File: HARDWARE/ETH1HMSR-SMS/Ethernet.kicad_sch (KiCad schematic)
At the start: 34 parts, among them J301 RJ45_Wuerth_7499010121A, U301 LAN8742A, Y301 NX5032GA-25

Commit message: SW and HW development
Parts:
- removed R302, R304, R305: 33, Resistor_SMD:R_0603_1608Metric_Pad0.98x0.95mm_HandSolder, symbol Device:R
- removed R303, R306, R307, R308, R309: 10k, Resistor_SMD:R_0603_1608Metric_Pad0.98x0.95mm_HandSolder, symbol Device:R
- removed R313, R314, R315, R316: 49R9, Resistor_SMD:R_0603_1608Metric_Pad0.98x0.95mm_HandSolder, symbol Device:R
- added RN301: EXB-V8V103JV, Resistor_SMD:R_Array_Concave_4x0603, symbol Device:R_Pack04
- added RN302: EXB-V8V330JV, Resistor_SMD:R_Array_Concave_4x0603, symbol Device:R_Pack04
- added RN303: EXB-38V510JV, Resistor_SMD:R_Array_Concave_4x0603, symbol Device:R_Pack04
- R301: value 33 -> 10k
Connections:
- net +3.3V: now also RN301.5 (R4.2), RN301.6 (R3.2), RN301.7 (R2.2), RN301.8 (R1.2)
- net ETH_RXN: now also RN303.4 (R4.1)
- net ETH_RXP: now also RN303.3 (R3.1)
- net ETH_TXN: now also RN303.2 (R2.1)
- net ETH_TXP: now also RN303.1 (R1.1)
- net GND: now also R301.1
- net MODE0: now also RN301.1 (R1.1), RN302.8 (R1.2); no longer R301.1
- net MODE1: now also RN301.2 (R2.1), RN302.7 (R2.2)
- net MODE2: now also RN301.3 (R3.1), RN302.6 (R3.2)
- net REFCLK0: now also RN301.4 (R4.1), RN302.5 (R4.2)
- net REF_CLK: now also RN302.4 (R4.1)
- net RMII_CRS_DV: now also RN302.3 (R3.1)
- net RMII_RXD0: now also RN302.1 (R1.1); no longer R301.2
- net RMII_RXD1: now also RN302.2 (R2.1)
- net VCCQ: now also RN303.5 (R4.2), RN303.6 (R3.2), RN303.7 (R2.2), RN303.8 (R1.2)
- net at U301.10 (RXER/PHYAD0): now also R301.2
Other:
- moved on the sheet: C301, C302, C303, C304, C305, C306, C307, C308, C309, C310, C311, C312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

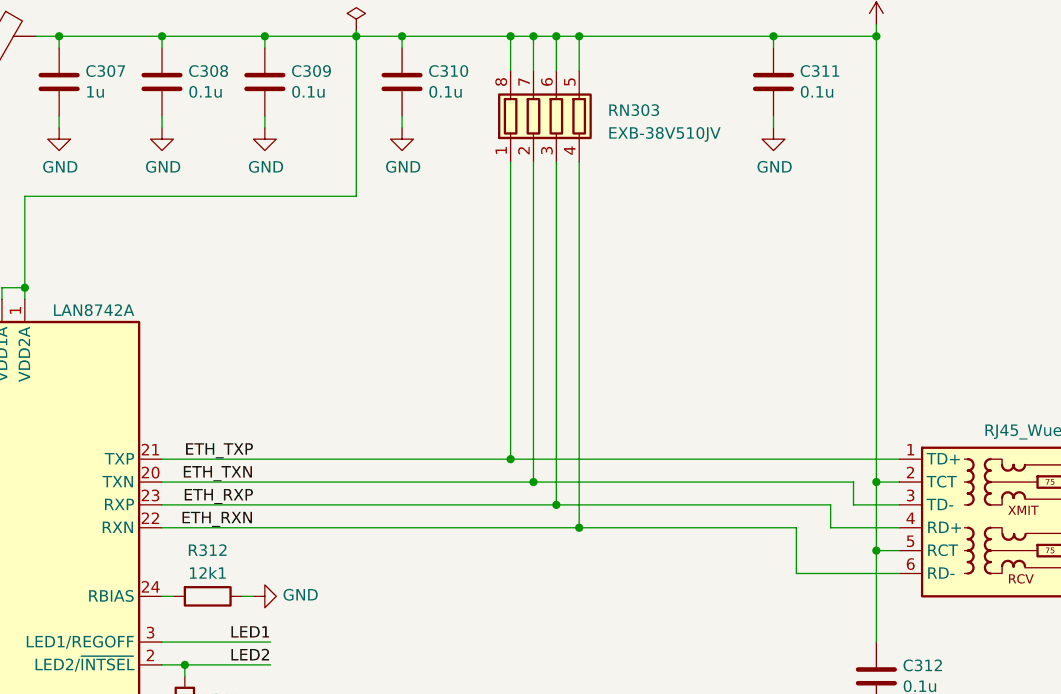
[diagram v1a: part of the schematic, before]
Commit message: Updated to Kicad 8
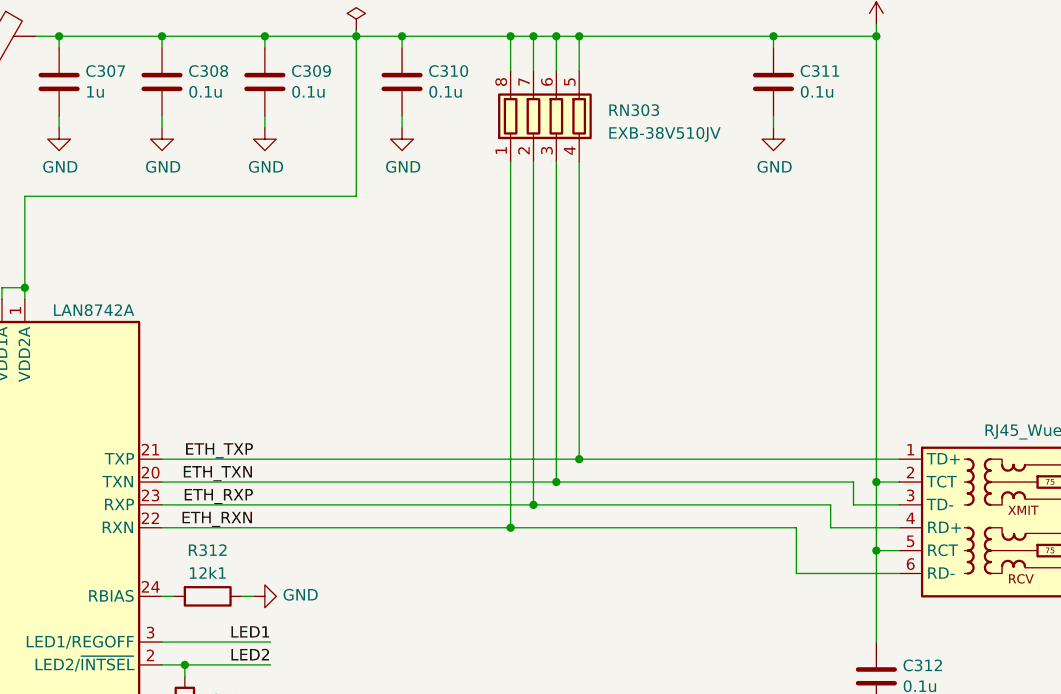
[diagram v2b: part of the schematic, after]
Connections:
- net ETH_RXN: now also RN303.1 (R1.1); no longer RN303.4 (R4.1)
- net ETH_RXP: now also RN303.2 (R2.1); no longer RN303.3 (R3.1)
- net ETH_TXN: now also RN303.3 (R3.1); no longer RN303.2 (R2.1)
- net ETH_TXP: now also RN303.4 (R4.1); no longer RN303.1 (R1.1)

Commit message: PCB design
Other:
- moved on the sheet: RN302
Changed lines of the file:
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@@
 	(wire
 		(pts
-			(xy 65.405 83.82) (xy 60.96 83.82)
+			(xy 67.31 83.82) (xy 60.96 83.82)
 		)
 		(stroke
@@
 	(wire
 		(pts
-			(xy 60.96 86.36) (xy 65.405 86.36)
+			(xy 60.96 86.36) (xy 67.31 86.36)
 		)
 		(stroke
@@
 	(wire
 		(pts
-			(xy 60.96 91.44) (xy 65.405 91.44)
+			(xy 60.96 91.44) (xy 67.31 91.44)
 		)
 		(stroke
@@
 	(wire
 		(pts
-			(xy 75.565 86.36) (xy 92.71 86.36)
+			(xy 77.47 86.36) (xy 92.71 86.36)
 		)
 		(stroke
@@
 	(wire
 		(pts
-			(xy 60.96 88.9) (xy 65.405 88.9)
+			(xy 60.96 88.9) (xy 67.31 88.9)
 		)
 		(stroke
@@
 	(wire
 		(pts
-			(xy 76.835 104.14) (xy 92.71 104.14)
+			(xy 78.74 104.14) (xy 92.71 104.14)
 		)
 		(stroke
@@
 	(wire
 		(pts
-			(xy 76.835 91.44) (xy 76.835 104.14)
+			(xy 78.74 91.44) (xy 78.74 104.14)
 		)
 		(stroke
@@
 	(wire
 		(pts
-			(xy 75.565 83.82) (xy 92.71 83.82)
+			(xy 77.47 83.82) (xy 92.71 83.82)
 		)
 		(stroke
@@
 	(wire
 		(pts
-			(xy 75.565 91.44) (xy 76.835 91.44)
+			(xy 77.47 91.44) (xy 78.74 91.44)
 		)
 		(stroke
@@
 	(wire
 		(pts
-			(xy 78.74 91.44) (xy 92.71 91.44)
+			(xy 80.01 91.44) (xy 92.71 91.44)
 		)
 		(stroke
@@
 	(wire
 		(pts
-			(xy 75.565 88.9) (xy 78.74 88.9)
+			(xy 77.47 88.9) (xy 80.01 88.9)
 		)
 		(stroke
@@
 	(wire
 		(pts
-			(xy 78.74 88.9) (xy 78.74 91.44)
+			(xy 80.01 88.9) (xy 80.01 91.44)
 		)
 		(stroke
@@
 	(symbol
 		(lib_id "Device:R_Pack04")
-		(at 70.485 88.9 270)
+		(at 72.39 88.9 270)
 		(unit 1)
 		(exclude_from_sim no)
@@
 		(dnp no)
 		(property "Reference" "RN302"
-			(at 64.135 82.55 90)
+			(at 64.516 82.55 90)
 			(effects
 				(font
@@
 		)
 		(property "Value" "EXB-V8V330JV"
-			(at 68.58 94.615 90)
+			(at 70.485 94.615 90)
 			(effects
 				(font
@@
 		)
 		(property "Footprint" "Resistor_SMD:R_Array_Concave_4x0603"
-			(at 70.485 95.885 90)
+			(at 72.39 95.885 90)
 			(effects
 				(font
@@
 		)
 		(property "Datasheet" "~"
-			(at 70.485 88.9 0)
+			(at 72.39 88.9 0)
 			(effects
 				(font
@@
 		)
 		(property "Description" ""
-			(at 70.485 88.9 0)
-			(effects
-				(font
+			(at 72.39 88.9 0)
+			(effects
+				(font

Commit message: Development
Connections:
- net LED1: now also J301.9; no longer J301.10
- net LED2: now also J301.11; no longer J301.12
- net at R317.1: now also J301.12; no longer J301.11
- net at R318.1: now also J301.10; no longer J301.9
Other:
- moved on the sheet: C301, C311, C312, J301, R301, R310, R317, R318, RN301, RN303

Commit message: PCB
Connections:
- net LED1: now also J301.10; no longer J301.9
- net LED2: now also J301.12; no longer J301.11
- net at R317.1: now also J301.11; no longer J301.12
- net at R318.1: now also J301.9; no longer J301.10
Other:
- moved on the sheet: R317, R318
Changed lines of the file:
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@@
 	(wire
 		(pts
-			(xy 256.54 88.9) (xy 257.81 88.9)
+			(xy 256.54 91.44) (xy 257.81 91.44)
 		)
 		(stroke
@@
 	(wire
 		(pts
-			(xy 256.54 78.74) (xy 257.81 78.74)
+			(xy 256.54 81.28) (xy 257.81 81.28)
 		)
 		(stroke
@@
 	(wire
 		(pts
-			(xy 273.05 82.55) (xy 257.81 82.55)
+			(xy 267.97 74.93) (xy 257.81 74.93)
 		)
 		(stroke
@@
 	(wire
 		(pts
-			(xy 257.81 81.28) (xy 256.54 81.28)
-		)
-		(stroke
-			(width 0)
-			(type default)
-		)
-	)
-	(wire
-		(pts
-			(xy 257.81 82.55) (xy 257.81 81.28)
-		)
-		(stroke
-			(width 0)
-			(type default)
-		)
-	)
-	(wire
-		(pts
 			(xy 210.82 31.75) (xy 210.82 81.28)
 		)
@@
 	(wire
 		(pts
+			(xy 257.81 78.74) (xy 257.81 74.93)
+		)
+		(stroke
+			(width 0)
+			(type default)
+		)
+	)
+	(wire
+		(pts
 			(xy 130.81 33.02) (xy 130.81 31.75)
 		)
@@
 	(wire
 		(pts
+			(xy 256.54 78.74) (xy 257.81 78.74)
+		)
+		(stroke
+			(width 0)
+			(type default)
+		)
+	)
+	(wire
+		(pts
 			(xy 152.4 31.75) (xy 142.24 31.75)
 		)
@@
 	(wire
 		(pts
-			(xy 273.05 92.71) (xy 257.81 92.71)
+			(xy 267.97 85.09) (xy 257.81 85.09)
 		)
 		(stroke
@@
 	(wire
 		(pts
-			(xy 257.81 92.71) (xy 257.81 91.44)
+			(xy 80.01 91.44) (xy 92.71 91.44)
 		)
 		(stroke
@@
 	(wire
 		(pts
-			(xy 80.01 91.44) (xy 92.71 91.44)
+			(xy 115.57 49.53) (xy 152.4 49.53)
 		)
 		(stroke
@@
 	(wire
 		(pts
-			(xy 115.57 49.53) (xy 152.4 49.53)
+			(xy 201.93 86.36) (xy 201.93 91.44)
 		)
 		(stroke
@@
 	(wire
 		(pts
-			(xy 201.93 86.36) (xy 201.93 91.44)
+			(xy 170.18 31.75) (xy 170.18 35.56)
 		)
 		(stroke
@@
 	(wire
 		(pts
-			(xy 170.18 31.75) (xy 170.18 35.56)
+			(xy 248.92 96.52) (xy 248.92 97.79)
 		)
 		(stroke
@@
 	(wire
 		(pts
-			(xy 248.92 96.52) (xy 248.92 97.79)
+			(xy 257.81 85.09) (xy 257.81 88.9)
 		)
 		(stroke
@@
 	(wire
 		(pts
-			(xy 77.47 88.9) (xy 80.01 88.9)
+			(xy 256.54 88.9) (xy 257.81 88.9)
 		)
 		(stroke
@@
 	(wire
 		(pts
-			(xy 172.72 83.82) (xy 205.74 83.82)
+			(xy 77.47 88.9) (xy 80.01 88.9)
 		)
 		(stroke
@@
 	(wire
 		(pts
-			(xy 96.52 162.56) (xy 99.06 162.56)
+			(xy 172.72 83.82) (xy 205.74 83.82)
 		)
 		(stroke
@@
 	(wire
 		(pts
-			(xy 205.74 86.36) (xy 213.36 86.36)
+			(xy 96.52 162.56) (xy 99.06 162.56)
 		)
 		(stroke
@@
 	(wire
 		(pts
-			(xy 257.81 91.44) (xy 256.54 91.44)
+			(xy 205.74 86.36) (xy 213.36 86.36)
 		)
 		(stroke
@@
 	)
 	(label "LED1"
-		(at 273.05 92.71 180)
+		(at 267.97 85.09 180)
 		(fields_autoplaced yes)
 		(effects
@@
 	)
 	(label "LED2"
-		(at 273.05 82.55 180)
+		(at 267.97 74.93 180)
 		(fields_autoplaced yes)
 		(effects
@@
 	(symbol
 		(lib_id "Device:R")
-		(at 261.62 78.74 90)
+		(at 261.62 81.28 90)
 		(unit 1)
 		(exclude_from_sim no)
@@
 		(dnp no)
 		(property "Reference" "R317"
-			(at 261.62 74.295 90)
+			(at 261.62 76.835 90)
 			(effects
 				(font
@@
 		)
 		(property "Value" "560"
-			(at 261.62 76.2 90)
+			(at 261.62 78.74 90)
 			(effects
 				(font
@@
 		)
 		(property "Footprint" "Resistor_SMD:R_0603_1608Metric_Pad0.98x0.95mm_HandSolder"
-			(at 261.62 80.518 90)
+			(at 261.62 83.058 90)
 			(effects
 				(font
@@
 		)
 		(property "Datasheet" "~"
-			(at 261.62 78.74 0)
+			(at 261.62 81.28 0)
 			(effects
 				(font
@@
 		)
 		(property "Description" ""
-			(at 261.62 78.74 0)
+			(at 261.62 81.28 0)
 			(effects
 				(font
@@
 	(symbol
 		(lib_id "power:GND")
-		(at 265.43 88.9 90)
+		(at 265.43 91.44 90)
 		(unit 1)
 		(exclude_from_sim no)
@@
 		(fields_autoplaced yes)
 		(property "Reference" "#PWR0322"
-			(at 271.78 88.9 0)
+			(at 271.78 91.44 0)
 			(effects
 				(font
@@
 		)
 		(property "Value" "GND"
-			(at 269.24 88.9 90)
+			(at 269.24 91.44 90)
 			(effects
 				(font
@@
 		)
 		(property "Footprint" ""
-			(at 265.43 88.9 0)
+			(at 265.43 91.44 0)
 			(effects
 				(font
@@
 		)
 		(property "Datasheet" ""
-			(at 265.43 88.9 0)
+			(at 265.43 91.44 0)
 			(effects
 				(font
@@
 		)
 		(property "Description" "Power symbol creates a global label with name \"GND\" , ground"
-			(at 265.43 88.9 0)
+			(at 265.43 91.44 0)
 			(effects
 				(font
@@
 	(symbol
 		(lib_id "Device:R")
-		(at 261.62 88.9 90)
+		(at 261.62 91.44 90)
 		(unit 1)
 		(exclude_from_sim no)
@@
 		(dnp no)
 		(property "Reference" "R318"
-			(at 261.62 84.455 90)
+			(at 261.62 86.995 90)
 			(effects
 				(font
@@
 		)
 		(property "Value" "560"
-			(at 261.62 86.36 90)
+			(at 261.62 88.9 90)
 			(effects
 				(font
@@
 		)
 		(property "Footprint" "Resistor_SMD:R_0603_1608Metric_Pad0.98x0.95mm_HandSolder"
-			(at 261.62 90.678 90)
+			(at 261.62 93.218 90)
 			(effects
 				(font
@@
 		)
 		(property "Datasheet" "~"
-			(at 261.62 88.9 0)
+			(at 261.62 91.44 0)
 			(effects
 				(font
@@
 		)
 		(property "Description" ""
-			(at 261.62 88.9 0)
+			(at 261.62 91.44 0)
 			(effects
 				(font
@@
 	(symbol
 		(lib_id "power:GND")
-		(at 265.43 78.74 90)
+		(at 265.43 81.28 90)
 		(unit 1)
 		(exclude_from_sim no)
@@
 		(fields_autoplaced yes)
 		(property "Reference" "#PWR0321"
-			(at 271.78 78.74 0)
+			(at 271.78 81.28 0)
 			(effects
 				(font
@@
 		)
 		(property "Value" "GND"
-			(at 269.24 78.74 90)
+			(at 269.24 81.28 90)
 			(effects
 				(font
@@
 		)
 		(property "Footprint" ""
-			(at 265.43 78.74 0)
+			(at 265.43 81.28 0)
 			(effects
 				(font
@@
 		)
 		(property "Datasheet" ""
-			(at 265.43 78.74 0)
+			(at 265.43 81.28 0)
 			(effects
 				(font
@@
 		)
 		(property "Description" "Power symbol creates a global label with name \"GND\" , ground"
-			(at 265.43 78.74 0)
+			(at 265.43 81.28 0)
 			(effects
 				(font

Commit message: development
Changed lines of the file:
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@@
 	(wire
 		(pts
-			(xy 60.96 96.52) (xy 82.55 96.52)
+			(xy 60.96 96.52) (xy 81.28 96.52)
 		)
 		(stroke
@@
 	(wire
 		(pts
-			(xy 82.55 96.52) (xy 82.55 93.98)
+			(xy 81.28 96.52) (xy 81.28 93.98)
 		)
 		(stroke
@@
 	(wire
 		(pts
-			(xy 82.55 93.98) (xy 92.71 93.98)
+			(xy 81.28 93.98) (xy 92.71 93.98)
 		)
 		(stroke
@@
 	)
 	(label "RMII_MDIO"
-		(at 82.55 93.98 0)
+		(at 81.28 93.98 0)
 		(fields_autoplaced yes)
 		(effects
@@
 	)
 	(label "MODE1"
-		(at 86.36 86.36 0)
+		(at 85.09 86.36 0)
 		(fields_autoplaced yes)
 		(effects
@@
 	)
 	(label "MODE2"
-		(at 86.36 91.44 0)
+		(at 85.09 91.44 0)
 		(fields_autoplaced yes)
 		(effects
@@
 	)
 	(label "MODE0"
-		(at 86.36 83.82 0)
+		(at 85.09 83.82 0)
 		(fields_autoplaced yes)
 		(effects
@@
 	)
 	(label "REFCLK0"
-		(at 83.82 104.14 0)
-		(fields_autoplaced yes)
-		(effects
+		(at 82.55 104.14 0)
+		(fields_autoplaced yes)
+		(effects
